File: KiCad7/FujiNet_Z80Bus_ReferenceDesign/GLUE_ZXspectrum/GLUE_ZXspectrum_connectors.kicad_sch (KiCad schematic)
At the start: 1 part

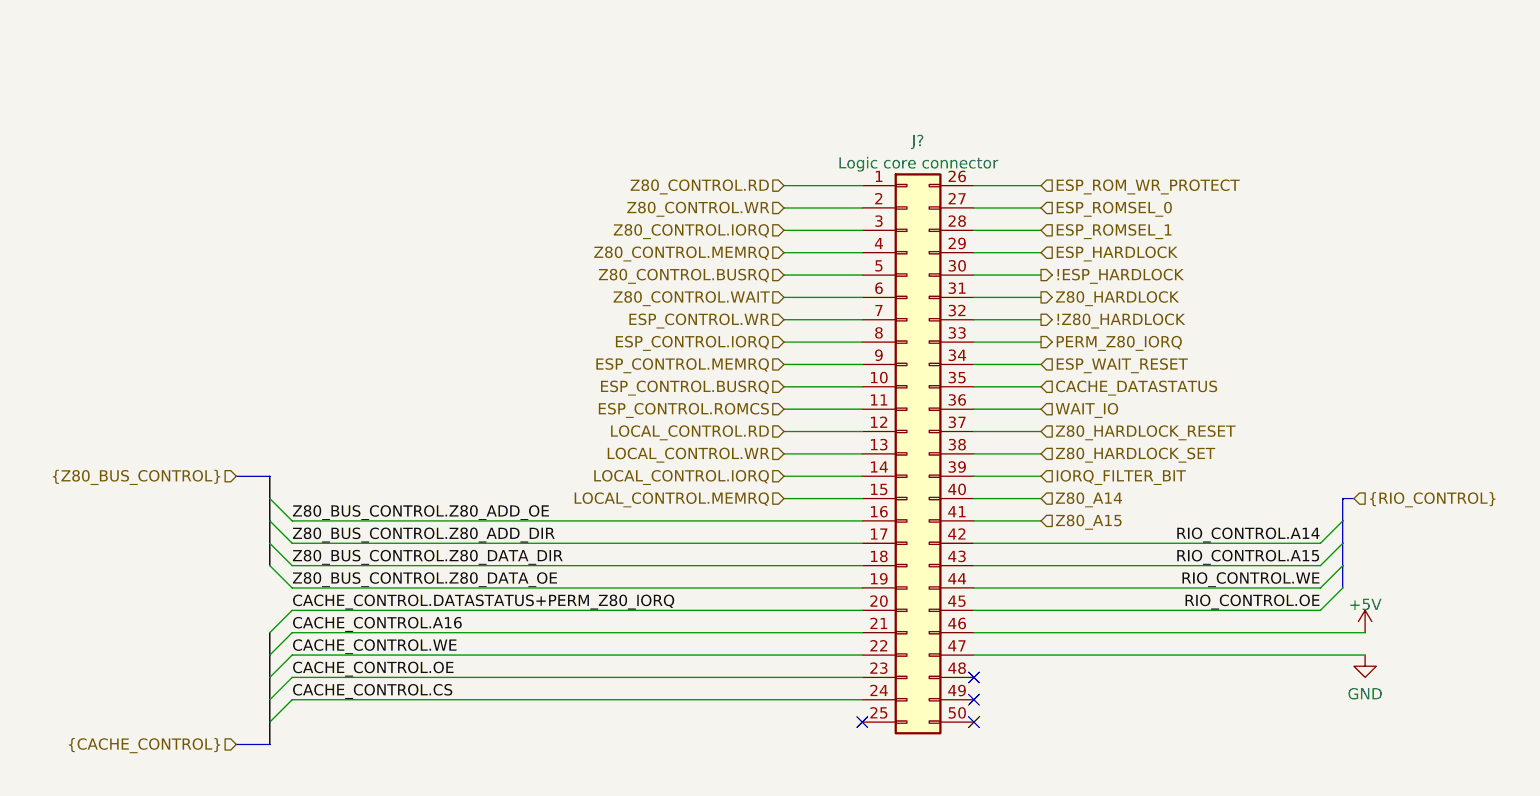
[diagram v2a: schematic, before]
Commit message: KiCad Prototype routing (failed)
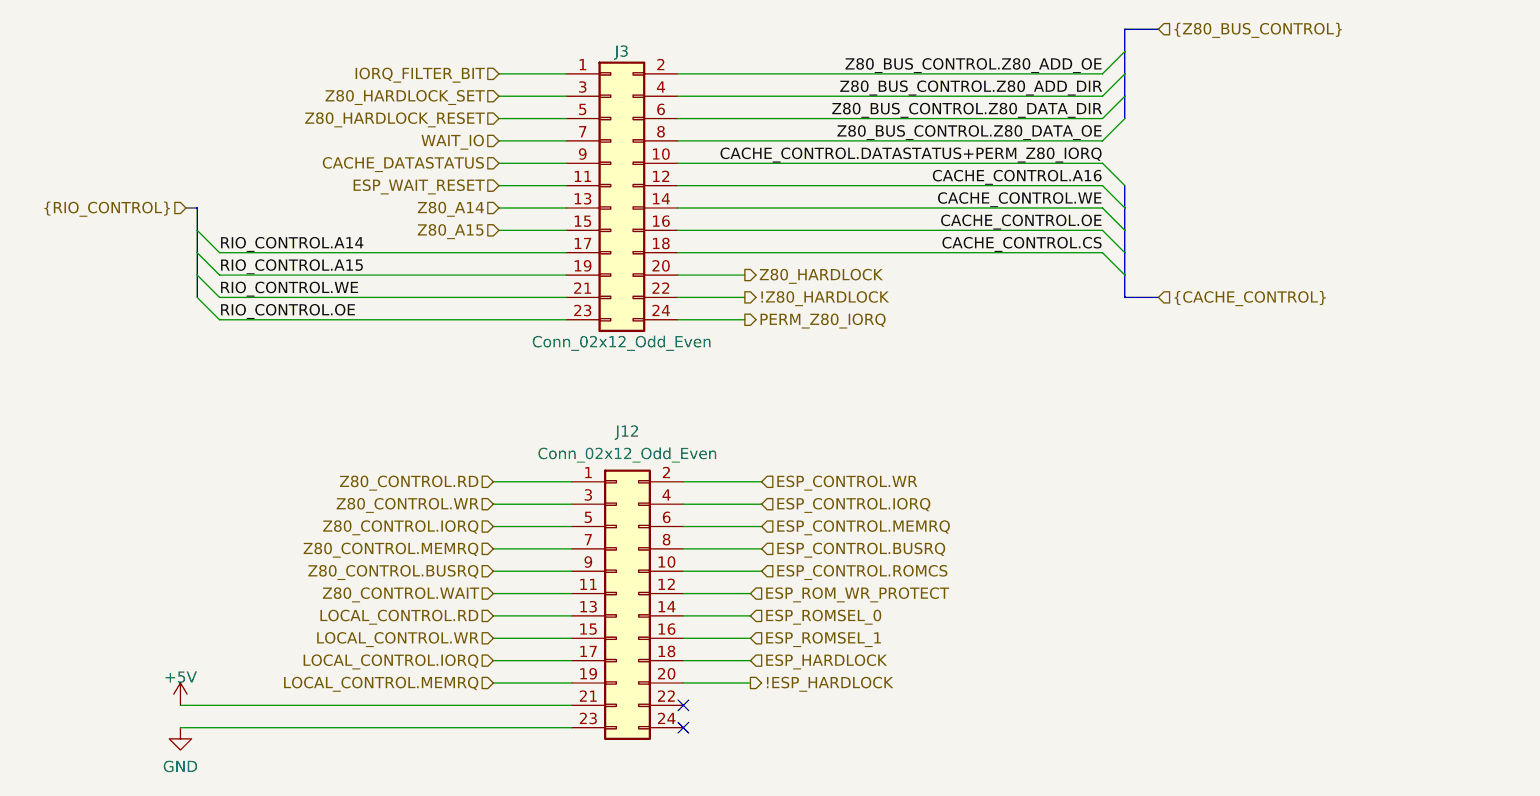
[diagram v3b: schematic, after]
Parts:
- removed J?: Logic core connector, Connector_PinHeader_2.54mm:PinHeader_2x25_P2.54mm_Vertical, symbol Connector_Generic:Conn_02x25_Top_Bottom
- added J12, J3: Conn_02x12_Odd_Even, Connector_PinHeader_2.54mm:PinHeader_2x16_P2.54mm_Vertical, symbol Connector_Generic:Conn_02x12_Odd_Even
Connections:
- net !ESP_HARDLOCK: now also J12.20 (Pin_20)
- net !Z80_HARDLOCK: now also J3.22 (Pin_22)
- net +5V: now also J12.21 (Pin_21)
- net CACHE_CONTROL.A16: now also J3.12 (Pin_12)
- net CACHE_CONTROL.CS: now also J3.18 (Pin_18)
- net CACHE_CONTROL.DATASTATUS+PERM_Z80_IORQ: now also J3.10 (Pin_10)
- net CACHE_CONTROL.OE: now also J3.16 (Pin_16)
- net CACHE_CONTROL.WE: now also J3.14 (Pin_14)
- net CACHE_DATASTATUS: now also J3.9 (Pin_9)
- net ESP_CONTROL.BUSRQ: now also J12.8 (Pin_8)
- net ESP_CONTROL.IORQ: now also J12.4 (Pin_4)
- net ESP_CONTROL.MEMRQ: now also J12.6 (Pin_6)
- net ESP_CONTROL.ROMCS: now also J12.10 (Pin_10)
- net ESP_CONTROL.WR: now also J12.2 (Pin_2)
- net ESP_HARDLOCK: now also J12.18 (Pin_18)
- net ESP_ROMSEL_0: now also J12.14 (Pin_14)
- net ESP_ROMSEL_1: now also J12.16 (Pin_16)
- net ESP_ROM_WR_PROTECT: now also J12.12 (Pin_12)
- net ESP_WAIT_RESET: now also J3.11 (Pin_11)
- net GND: now also J12.23 (Pin_23)
- net IORQ_FILTER_BIT: now also J3.1 (Pin_1)
- net LOCAL_CONTROL.IORQ: now also J12.17 (Pin_17)
- net LOCAL_CONTROL.MEMRQ: now also J12.19 (Pin_19)
- net LOCAL_CONTROL.RD: now also J12.13 (Pin_13)
- net LOCAL_CONTROL.WR: now also J12.15 (Pin_15)
- net PERM_Z80_IORQ: now also J3.24 (Pin_24)
- net RIO_CONTROL.A14: now also J3.17 (Pin_17)
- net RIO_CONTROL.A15: now also J3.19 (Pin_19)
- net RIO_CONTROL.OE: now also J3.23 (Pin_23)
- net RIO_CONTROL.WE: now also J3.21 (Pin_21)
- net WAIT_IO: now also J3.7 (Pin_7)
- net Z80_A14: now also J3.13 (Pin_13)
- net Z80_A15: now also J3.15 (Pin_15)
- net Z80_BUS_CONTROL.Z80_ADD_DIR: now also J3.4 (Pin_4)
- net Z80_BUS_CONTROL.Z80_ADD_OE: now also J3.2 (Pin_2)
- net Z80_BUS_CONTROL.Z80_DATA_DIR: now also J3.6 (Pin_6)
- net Z80_BUS_CONTROL.Z80_DATA_OE: now also J3.8 (Pin_8)
- net Z80_CONTROL.BUSRQ: now also J12.9 (Pin_9)
- net Z80_CONTROL.IORQ: now also J12.5 (Pin_5)
- net Z80_CONTROL.MEMRQ: now also J12.7 (Pin_7)
- net Z80_CONTROL.RD: now also J12.1 (Pin_1)
- net Z80_CONTROL.WAIT: now also J12.11 (Pin_11)
- net Z80_CONTROL.WR: now also J12.3 (Pin_3)
- net Z80_HARDLOCK: now also J3.20 (Pin_20)
- net Z80_HARDLOCK_RESET: now also J3.5 (Pin_5)
- net Z80_HARDLOCK_SET: now also J3.3 (Pin_3)
- no-connect marks 4 -> 2
